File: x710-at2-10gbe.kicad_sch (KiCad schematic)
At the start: 22 parts, among them U9 EZX710AT2_S_LMR5

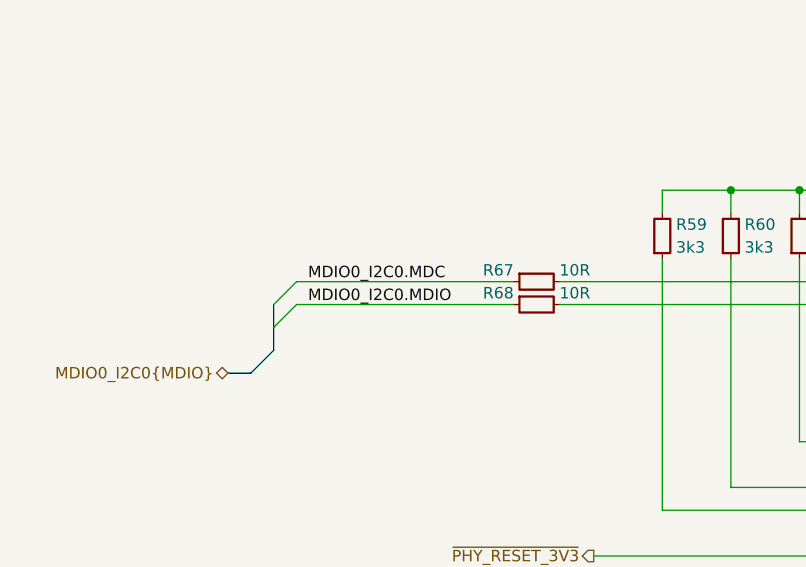
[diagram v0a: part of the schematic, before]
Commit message: [#86617] Power U10 from OCuLink, remove JTAG sheet pin, fix I2C cross
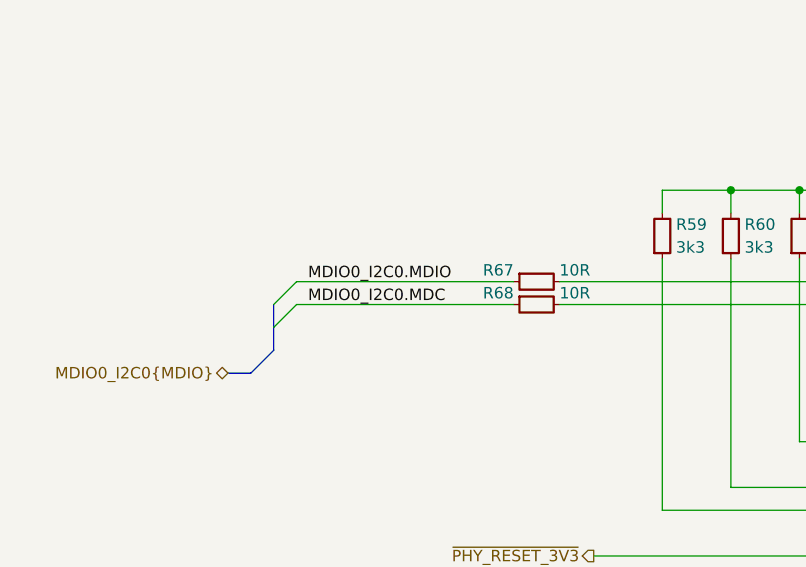
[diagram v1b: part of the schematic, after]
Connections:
- net MDIO0_I2C0.MDC: now also R68.1; no longer R67.1
- net MDIO0_I2C0.MDIO: now also R67.1; no longer R68.1
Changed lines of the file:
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@@
+		)
+	)
+	(label "MDIO0_I2C0.MDIO"
+		(at 82.55 167.64 0)
+		(effects
+			(font
+				(size 1.27 1.27)
+			)
+			(justify left bottom)
 		)
 	)
@@
 		)
 	)
-	(label "MDIO0_I2C0.MDIO"
-		(at 82.55 170.18 0)
-		(effects
-			(font
-				(size 1.27 1.27)
-			)
-			(justify left bottom)
-		)
-	)
 	(label "Ethernet_P0.D2+"
 		(at 190.5 60.96 180)
@@
 		)
 	)
-	(label "MDIO0_I2C0.MDC"
-		(at 82.55 167.64 0)
-		(effects
-			(font
-				(size 1.27 1.27)
-			)
-			(justify left bottom)
-		)
-	)
 	(label "Ethernet_P0.D3-"
 		(at 190.5 71.12 180)
@@
 		(effects
 			(font
+				(size 1.27 1.27)
+			)
+			(justify left bottom)
+		)
+	)
+	(label "MDIO0_I2C0.MDC"
+		(at 82.55 170.18 0)
+		(effects
+			(font

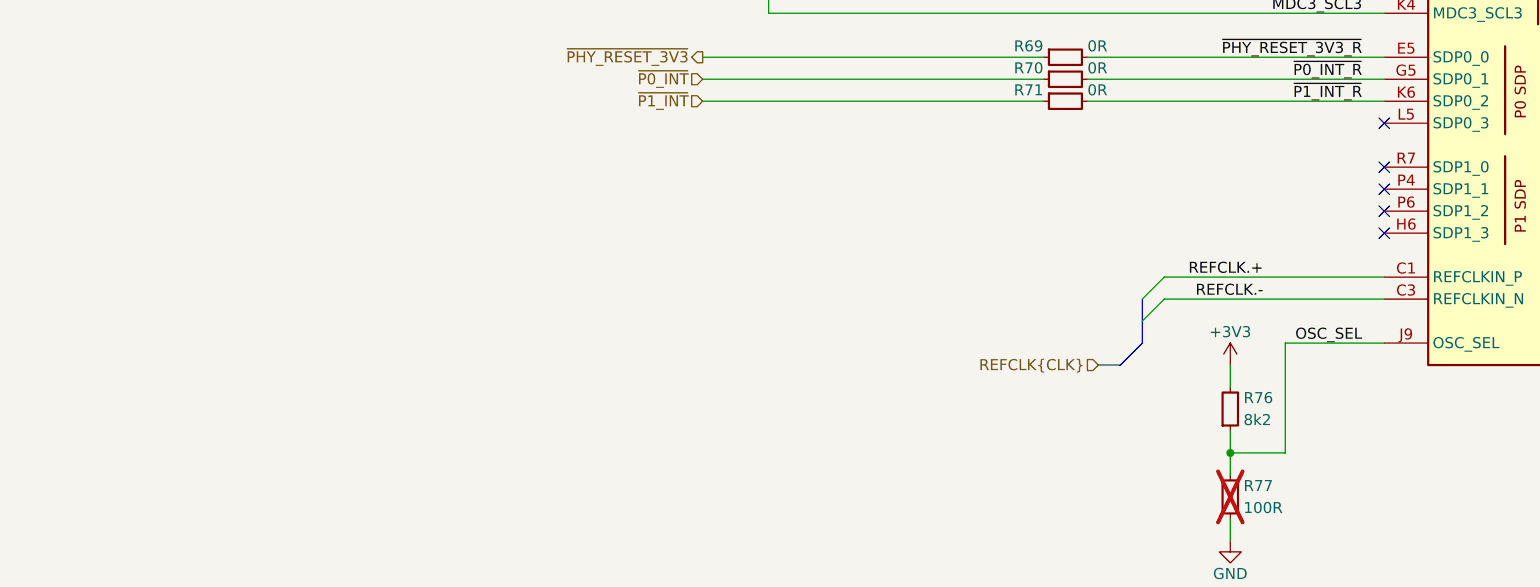
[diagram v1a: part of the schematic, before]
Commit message: [#86617] Remove misc schematic sheet
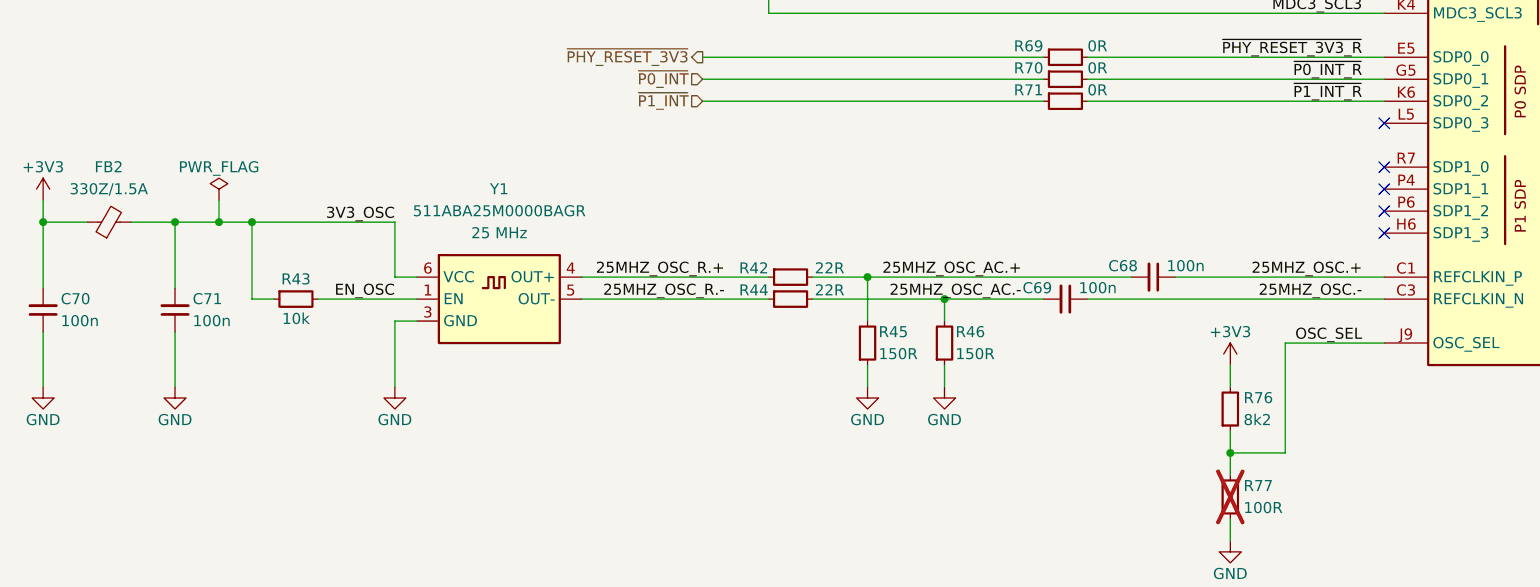
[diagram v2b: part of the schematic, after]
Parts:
- added C68, C69, C70, C71: C_100n_16V_X7R_0402, antmicro-footprints:C_0402_1005Metric, symbol antmicroCapacitors0402:C_100n_16V_X7R_0402
- added FB2: FB_330Z_1.5A_Murata-BLM21PG_0805, antmicro-footprints:FB_0805_2012Metric, symbol antmicroFerriteBeadsandChips:FB_330Z_1.5A_Murata-BLM21PG_0805
- added R42, R44: R_22R_0402, antmicro-footprints:R_0402_1005Metric, symbol antmicroResistors0402:R_22R_0402
- added R43: R_10k_0402, antmicro-footprints:R_0402_1005Metric, symbol antmicroResistors0402:R_10k_0402
- added R45, R46: R_150R_0402, antmicro-footprints:R_0402_1005Metric, symbol antmicroResistors0402:R_150R_0402
- added Y1: Oscillator_25MHz_511ABA25M0000BAGR, antmicro-footprints:Oscillator_SMD_Skyworks_SI511_5x3.2x1.17mm, symbol antmicroOscillators:Oscillator_25MHz_511ABA25M0000BAGR
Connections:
- net +3V3: now also C70.2, FB2.1
- net GND: now also C70.1, C71.1, R45.1, R46.1, Y1.3 (GND)
- net REFCLK.+ renamed 25MHZ_OSC.+
- net 25MHZ_OSC.+: now also C68.1
- net REFCLK.- renamed 25MHZ_OSC.-
- net 25MHZ_OSC.-: now also C69.1
- new net 25MHZ_OSC_AC.+: C68.2, R42.2, R45.2
- new net 25MHZ_OSC_AC.-: C69.2, R44.2, R46.2
- new net 25MHZ_OSC_R.+: R42.1, Y1.4 (OUT+)
- new net 25MHZ_OSC_R.-: R44.1, Y1.5 (OUT-)
- new net 3V3_OSC: C71.2, FB2.2, R43.1, Y1.6 (VCC)
- new net EN_OSC: R43.2, Y1.1 (EN)

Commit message: [#86351] Rename project
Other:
- title: 10GbE Expansion -> OCuLink to 10GbE adapter
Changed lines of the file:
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@@
 	(paper "A3")
 	(title_block
-		(title "10GbE Expansion")
+		(title "OCuLink to 10GbE adapter")
 		(date "2025-11-07")
 		(rev "1.0.0")
@@
 		)
 		(instances
-			(project "10-gbe-expansion"
+			(project "OCuLink to 10GbE adapter"
 				(path "/04bda987-e5eb-48b4-9e90-d8211dc11b39/46fcd652-659b-4e06-aa16-4947b5e55b68"
 					(reference "#PWR0251")
@@
 		)
 		(instances
-			(project "10-gbe-expansion"
+			(project "OCuLink to 10GbE adapter"
 				(path "/04bda987-e5eb-48b4-9e90-d8211dc11b39/46fcd652-659b-4e06-aa16-4947b5e55b68"
 					(reference "C71")
@@
 		)
 		(instances
-			(project "10-gbe-expansion"
+			(project "OCuLink to 10GbE adapter"
 				(path "/04bda987-e5eb-48b4-9e90-d8211dc11b39/46fcd652-659b-4e06-aa16-4947b5e55b68"
 					(reference "R46")
@@
 		)
 		(instances
-			(project "10-gbe-expansion"
+			(project "OCuLink to 10GbE adapter"
 				(path "/04bda987-e5eb-48b4-9e90-d8211dc11b39/46fcd652-659b-4e06-aa16-4947b5e55b68"
 					(reference "C68")
@@
 		)
 		(instances
-			(project "10-gbe-expansion"
+			(project "OCuLink to 10GbE adapter"
 				(path "/04bda987-e5eb-48b4-9e90-d8211dc11b39/46fcd652-659b-4e06-aa16-4947b5e55b68"
 					(reference "R71")
@@
 		)
 		(instances
-			(project "10-gbe-expansion"
+			(project "OCuLink to 10GbE adapter"
 				(path "/04bda987-e5eb-48b4-9e90-d8211dc11b39/46fcd652-659b-4e06-aa16-4947b5e55b68"
 					(reference "R66")
@@
 		)
 		(instances
-			(project "10-gbe-expansion"
+			(project "OCuLink to 10GbE adapter"
 				(path "/04bda987-e5eb-48b4-9e90-d8211dc11b39/46fcd652-659b-4e06-aa16-4947b5e55b68"
 					(reference "#PWR092")
@@
 		)
 		(instances
-			(project "10-gbe-expansion"
+			(project "OCuLink to 10GbE adapter"
 				(path "/04bda987-e5eb-48b4-9e90-d8211dc11b39/46fcd652-659b-4e06-aa16-4947b5e55b68"
 					(reference "#PWR0252")
@@
 		)
 		(instances
-			(project "10-gbe-expansion"
+			(project "OCuLink to 10GbE adapter"
 				(path "/04bda987-e5eb-48b4-9e90-d8211dc11b39/46fcd652-659b-4e06-aa16-4947b5e55b68"
 					(reference "R63")
@@
 		)
 		(instances
-			(project "10-gbe-expansion"
+			(project "OCuLink to 10GbE adapter"
 				(path "/04bda987-e5eb-48b4-9e90-d8211dc11b39/46fcd652-659b-4e06-aa16-4947b5e55b68"
 					(reference "R65")
@@
 		)
 		(instances
-			(project "10-gbe-expansion"
+			(project "OCuLink to 10GbE adapter"
 				(path "/04bda987-e5eb-48b4-9e90-d8211dc11b39/46fcd652-659b-4e06-aa16-4947b5e55b68"
 					(reference "#PWR0256")
@@
 		)
 		(instances
-			(project "10-gbe-expansion"
+			(project "OCuLink to 10GbE adapter"
 				(path "/04bda987-e5eb-48b4-9e90-d8211dc11b39/46fcd652-659b-4e06-aa16-4947b5e55b68"
 					(reference "R43")
@@
 		)
 		(instances
-			(project "10-gbe-expansion"
+			(project "OCuLink to 10GbE adapter"
 				(path "/04bda987-e5eb-48b4-9e90-d8211dc11b39/46fcd652-659b-4e06-aa16-4947b5e55b68"
 					(reference "R70")
@@
 		)
 		(instances
-			(project "10-gbe-expansion"
+			(project "OCuLink to 10GbE adapter"
 				(path "/04bda987-e5eb-48b4-9e90-d8211dc11b39/46fcd652-659b-4e06-aa16-4947b5e55b68"
 					(reference "R45")
@@
 		)
 		(instances
-			(project "10-gbe-expansion"
+			(project "OCuLink to 10GbE adapter"
 				(path "/04bda987-e5eb-48b4-9e90-d8211dc11b39/46fcd652-659b-4e06-aa16-4947b5e55b68"
 					(reference "#PWR0254")
@@
 		)
 		(instances
-			(project "10-gbe-expansion"
+			(project "OCuLink to 10GbE adapter"
 				(path "/04bda987-e5eb-48b4-9e90-d8211dc11b39/46fcd652-659b-4e06-aa16-4947b5e55b68"
 					(reference "#PWR0250")
@@
 		)
 		(instances
-			(project "10-gbe-expansion"
+			(project "OCuLink to 10GbE adapter"
 				(path "/04bda987-e5eb-48b4-9e90-d8211dc11b39/46fcd652-659b-4e06-aa16-4947b5e55b68"
 					(reference "C70")
@@
 		)
 		(instances
-			(project "10-gbe-expansion"
+			(project "OCuLink to 10GbE adapter"
 				(path "/04bda987-e5eb-48b4-9e90-d8211dc11b39/46fcd652-659b-4e06-aa16-4947b5e55b68"
 					(reference "R68")
@@
 		)
 		(instances
-			(project "10-gbe-expansion"
+			(project "OCuLink to 10GbE adapter"
 				(path "/04bda987-e5eb-48b4-9e90-d8211dc11b39/46fcd652-659b-4e06-aa16-4947b5e55b68"
 					(reference "R42")
@@
 		)
 		(instances
-			(project "10-gbe-expansion"
+			(project "OCuLink to 10GbE adapter"
 				(path "/04bda987-e5eb-48b4-9e90-d8211dc11b39/46fcd652-659b-4e06-aa16-4947b5e55b68"
 					(reference "#PWR093")
@@
 		)
 		(instances
-			(project "10-gbe-expansion"
+			(project "OCuLink to 10GbE adapter"
 				(path "/04bda987-e5eb-48b4-9e90-d8211dc11b39/46fcd652-659b-4e06-aa16-4947b5e55b68"
 					(reference "#PWR0257")
@@
 		)
 		(instances
-			(project "10-gbe-expansion"
+			(project "OCuLink to 10GbE adapter"
 				(path "/04bda987-e5eb-48b4-9e90-d8211dc11b39/46fcd652-659b-4e06-aa16-4947b5e55b68"
 					(reference "R58")
@@
 		)
 		(instances
-			(project "10-gbe-expansion"
+			(project "OCuLink to 10GbE adapter"
 				(path "/04bda987-e5eb-48b4-9e90-d8211dc11b39/46fcd652-659b-4e06-aa16-4947b5e55b68"
 					(reference "FB2")
@@
 		)
 		(instances
-			(project "10-gbe-expansion"
+			(project "OCuLink to 10GbE adapter"
 				(path "/04bda987-e5eb-48b4-9e90-d8211dc11b39/46fcd652-659b-4e06-aa16-4947b5e55b68"
 					(reference "R75")
@@
 		)
 		(instances
-			(project "10-gbe-expansion"
+			(project "OCuLink to 10GbE adapter"
 				(path "/04bda987-e5eb-48b4-9e90-d8211dc11b39/46fcd652-659b-4e06-aa16-4947b5e55b68"
 					(reference "Y1")
@@
 		)
 		(instances
-			(project "10-gbe-expansion"
+			(project "OCuLink to 10GbE adapter"
 				(path "/04bda987-e5eb-48b4-9e90-d8211dc11b39/46fcd652-659b-4e06-aa16-4947b5e55b68"
 					(reference "R44")
@@
 		)
 		(instances
-			(project "10-gbe-expansion"
+			(project "OCuLink to 10GbE adapter"
 				(path "/04bda987-e5eb-48b4-9e90-d8211dc11b39/46fcd652-659b-4e06-aa16-4947b5e55b68"
 					(reference "#PWR0253")
@@
 		)
 		(instances
-			(project "10-gbe-expansion"
+			(project "OCuLink to 10GbE adapter"
 				(path "/04bda987-e5eb-48b4-9e90-d8211dc11b39/46fcd652-659b-4e06-aa16-4947b5e55b68"
 					(reference "R57")
@@
 		)
 		(instances
-			(project "10-gbe-expansion"
+			(project "OCuLink to 10GbE adapter"
 				(path "/04bda987-e5eb-48b4-9e90-d8211dc11b39/46fcd652-659b-4e06-aa16-4947b5e55b68"
 					(reference "C69")
@@
 		)
 		(instances
-			(project "10-gbe-expansion"
+			(project "OCuLink to 10GbE adapter"
 				(path "/04bda987-e5eb-48b4-9e90-d8211dc11b39/46fcd652-659b-4e06-aa16-4947b5e55b68"
 					(reference "R74")
@@
 		)
 		(instances
-			(project "10-gbe-expansion"
+			(project "OCuLink to 10GbE adapter"
 				(path "/04bda987-e5eb-48b4-9e90-d8211dc11b39/46fcd652-659b-4e06-aa16-4947b5e55b68"
 					(reference "R61")
@@
 		)
 		(instances
-			(project "10-gbe-expansion"
+			(project "OCuLink to 10GbE adapter"
 				(path "/04bda987-e5eb-48b4-9e90-d8211dc11b39/46fcd652-659b-4e06-aa16-4947b5e55b68"
 					(reference "R72")
@@
 		)
 		(instances
-			(project "10-gbe-expansion"
+			(project "OCuLink to 10GbE adapter"
 				(path "/04bda987-e5eb-48b4-9e90-d8211dc11b39/46fcd652-659b-4e06-aa16-4947b5e55b68"
 					(reference "#PWR091")
@@
 		)
 		(instances
-			(project "10-gbe-expansion"
+			(project "OCuLink to 10GbE adapter"
 				(path "/04bda987-e5eb-48b4-9e90-d8211dc11b39/46fcd652-659b-4e06-aa16-4947b5e55b68"
 					(reference "#PWR094")
@@
 		)
 		(instances
-			(project "10-gbe-expansion"
+			(project "OCuLink to 10GbE adapter"
 				(path "/04bda987-e5eb-48b4-9e90-d8211dc11b39/46fcd652-659b-4e06-aa16-4947b5e55b68"
 					(reference "#PWR0255")
@@
 		)
 		(instances
-			(project "10-gbe-expansion"
+			(project "OCuLink to 10GbE adapter"
 				(path "/04bda987-e5eb-48b4-9e90-d8211dc11b39/46fcd652-659b-4e06-aa16-4947b5e55b68"
 					(reference "#FLG011")
@@
 		)
 		(instances
-			(project "10-gbe-expansion"
+			(project "OCuLink to 10GbE adapter"
 				(path "/04bda987-e5eb-48b4-9e90-d8211dc11b39/46fcd652-659b-4e06-aa16-4947b5e55b68"
 					(reference "R60")
@@
 		)
 		(instances
-			(project "10-gbe-expansion"
+			(project "OCuLink to 10GbE adapter"
 				(path "/04bda987-e5eb-48b4-9e90-d8211dc11b39/46fcd652-659b-4e06-aa16-4947b5e55b68"
 					(reference "#PWR090")
@@
 		)
 		(instances
-			(project "10-gbe-expansion"
+			(project "OCuLink to 10GbE adapter"
 				(path "/04bda987-e5eb-48b4-9e90-d8211dc11b39/46fcd652-659b-4e06-aa16-4947b5e55b68"
 					(reference "R59")
@@
 		)
 		(instances
-			(project "10-gbe-expansion"
+			(project "OCuLink to 10GbE adapter"
 				(path "/04bda987-e5eb-48b4-9e90-d8211dc11b39/46fcd652-659b-4e06-aa16-4947b5e55b68"
 					(reference "R64")
@@
 		)
 		(instances
-			(project "10-gbe-expansion"
+			(project "OCuLink to 10GbE adapter"
 				(path "/04bda987-e5eb-48b4-9e90-d8211dc11b39/46fcd652-659b-4e06-aa16-4947b5e55b68"
 					(reference "#PWR089")
@@
 		)
 		(instances
-			(project "10-gbe-expansion"
+			(project "OCuLink to 10GbE adapter"
 				(path "/04bda987-e5eb-48b4-9e90-d8211dc11b39/46fcd652-659b-4e06-aa16-4947b5e55b68"
 					(reference "R73")

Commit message: [#86351] Minor BOM consolidation
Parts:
- C68, C69, C70, C71: value C_100n_16V_X7R_0402 -> C_100n_0402; symbol antmicroCapacitors0402:C_100n_16V_X7R_0402 -> antmicroCapacitors0402:C_100n_0402; Dielectric X7R -> X5R; MPN C0402C104J4RAC7411 -> GRM155R61H104KE14D; Manufacturer KEMET -> Murata; Voltage 16V -> 50V
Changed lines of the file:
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@@
 	)
 	(symbol
-		(lib_id "antmicroCapacitors0402:C_100n_16V_X7R_0402")
+		(lib_id "antmicroCapacitors0402:C_100n_0402")
 		(at 53.34 229.87 90)
 		(unit 1)
@@
 			)
 		)
-		(property "Value" "C_100n_16V_X7R_0402"
+		(property "Value" "C_100n_0402"
 			(at 76.2 214.63 0)
 			(effects
@@
 			)
 		)
-		(property "Datasheet" "https://www.kemet.com/en/us/capacitors/product/C0402C104J4RAC7411.html"
+		(property "Datasheet" "https://www.murata.com/products/productdetail?partno=GRM155R61H104KE14%23"
 			(at 81.28 214.63 0)
 			(effects
@@
 			)
 		)
-		(property "Description" "SMD Multilayer Ceramic Capacitor, 100nF, 50V, 0402, ±5%, X7R"
+		(property "Description" "SMD Multilayer Ceramic Capacitor, 0.1 µF, 50 V, 0402 [1005 Metric], ± 10%, X5R, GRM Series"
 			(at 53.34 229.87 0)
 			(effects
@@
 			)
 		)
-		(property "MPN" "C0402C104J4RAC7411"
+		(property "MPN" "GRM155R61H104KE14D"
 			(at 83.82 214.63 0)
 			(effects
@@
 			)
 		)
-		(property "Voltage" "16V"
+		(property "Voltage" "50V"
 			(at 63.5 214.63 0)
 			(effects
@@
 			)
 		)
-		(property "Dielectric" "X7R"
+		(property "Dielectric" "X5R"
 			(at 66.04 214.63 0)
 			(effects
@@
 			)
 		)
-		(property "Manufacturer" "KEMET"
+		(property "Manufacturer" "Murata"
 			(at 68.58 214.63 0)
 			(effects
@@
 	)
 	(symbol
-		(lib_id "antmicroCapacitors0402:C_100n_16V_X7R_0402")
+		(lib_id "antmicroCapacitors0402:C_100n_0402")
 		(at 168.91 223.52 180)
 		(unit 1)
@@
 			)
 		)
-		(property "Value" "C_100n_16V_X7R_0402"
+		(property "Value" "C_100n_0402"
 			(at 153.67 200.66 0)
 			(effects
@@
 			)
 		)
-		(property "Datasheet" "https://www.kemet.com/en/us/capacitors/product/C0402C104J4RAC7411.html"
+		(property "Datasheet" "https://www.murata.com/products/productdetail?partno=GRM155R61H104KE14%23"
 			(at 153.67 195.58 0)
 			(effects
@@
 			)
 		)
-		(property "Description" "SMD Multilayer Ceramic Capacitor, 100nF, 50V, 0402, ±5%, X7R"
+		(property "Description" "SMD Multilayer Ceramic Capacitor, 0.1 µF, 50 V, 0402 [1005 Metric], ± 10%, X5R, GRM Series"
 			(at 168.91 223.52 0)
 			(effects
@@
 			)
 		)
-		(property "MPN" "C0402C104J4RAC7411"
+		(property "MPN" "GRM155R61H104KE14D"
 			(at 153.67 193.04 0)
 			(effects
@@
 			)
 		)
-		(property "Voltage" "16V"
+		(property "Voltage" "50V"
 			(at 153.67 213.36 0)
 			(effects
@@
 			)
 		)
-		(property "Dielectric" "X7R"
+		(property "Dielectric" "X5R"
 			(at 153.67 210.82 0)
 			(effects
@@
 			)
 		)
-		(property "Manufacturer" "KEMET"
+		(property "Manufacturer" "Murata"
 			(at 153.67 208.28 0)
 			(effects
@@
 	)
 	(symbol
-		(lib_id "antmicroCapacitors0402:C_100n_16V_X7R_0402")
+		(lib_id "antmicroCapacitors0402:C_100n_0402")
 		(at 38.1 229.87 90)
 		(unit 1)
@@
 			)
 		)
-		(property "Value" "C_100n_16V_X7R_0402"
+		(property "Value" "C_100n_0402"
 			(at 60.96 214.63 0)
 			(effects
@@
 			)
 		)
-		(property "Datasheet" "https://www.kemet.com/en/us/capacitors/product/C0402C104J4RAC7411.html"
+		(property "Datasheet" "https://www.murata.com/products/productdetail?partno=GRM155R61H104KE14%23"
 			(at 66.04 214.63 0)
 			(effects
@@
 			)
 		)
-		(property "Description" "SMD Multilayer Ceramic Capacitor, 100nF, 50V, 0402, ±5%, X7R"
+		(property "Description" "SMD Multilayer Ceramic Capacitor, 0.1 µF, 50 V, 0402 [1005 Metric], ± 10%, X5R, GRM Series"
 			(at 38.1 229.87 0)
 			(effects
@@
 			)
 		)
-		(property "MPN" "C0402C104J4RAC7411"
+		(property "MPN" "GRM155R61H104KE14D"
 			(at 68.58 214.63 0)
 			(effects
@@
 			)
 		)
-		(property "Voltage" "16V"
+		(property "Voltage" "50V"
 			(at 48.26 214.63 0)
 			(effects
@@
 			)
 		)
-		(property "Dielectric" "X7R"
+		(property "Dielectric" "X5R"
 			(at 50.8 214.63 0)
 			(effects
@@
 			)
 		)
-		(property "Manufacturer" "KEMET"
+		(property "Manufacturer" "Murata"
 			(at 53.34 214.63 0)
 			(effects
@@
 	)
 	(symbol
-		(lib_id "antmicroCapacitors0402:C_100n_16V_X7R_0402")
+		(lib_id "antmicroCapacitors0402:C_100n_0402")
 		(at 158.75 226.06 180)
 		(unit 1)
@@
 			)
 		)
-		(property "Value" "C_100n_16V_X7R_0402"
+		(property "Value" "C_100n_0402"
 			(at 143.51 203.2 0)
 			(effects
@@
 			)
 		)
-		(property "Datasheet" "https://www.kemet.com/en/us/capacitors/product/C0402C104J4RAC7411.html"
+		(property "Datasheet" "https://www.murata.com/products/productdetail?partno=GRM155R61H104KE14%23"
 			(at 143.51 198.12 0)
 			(effects
@@
 			)
 		)
-		(property "Description" "SMD Multilayer Ceramic Capacitor, 100nF, 50V, 0402, ±5%, X7R"
+		(property "Description" "SMD Multilayer Ceramic Capacitor, 0.1 µF, 50 V, 0402 [1005 Metric], ± 10%, X5R, GRM Series"
 			(at 158.75 226.06 0)
 			(effects
@@
 			)
 		)
-		(property "MPN" "C0402C104J4RAC7411"
+		(property "MPN" "GRM155R61H104KE14D"
 			(at 143.51 195.58 0)
 			(effects
@@
 			)
 		)
-		(property "Voltage" "16V"
+		(property "Voltage" "50V"
 			(at 143.51 215.9 0)
 			(effects
@@
 			)
 		)
-		(property "Dielectric" "X7R"
+		(property "Dielectric" "X5R"
 			(at 143.51 213.36 0)
 			(effects
@@
 			)
 		)
-		(property "Manufacturer" "KEMET"
+		(property "Manufacturer" "Murata"
 			(at 143.51 210.82 0)
 			(effects
